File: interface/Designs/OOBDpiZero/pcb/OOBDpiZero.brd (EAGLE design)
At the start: 73.5 x 42 mm, 132 parts, among them IC1 EEPROM24, IC100 LM1117MPX-3.3, IC2 DS3231, Q1 12MHz, U1 MAX98357, U100 SY6280, U101 SN65HVD230(SO8), U102 SN65HVD230(SO8), U2 MP1482

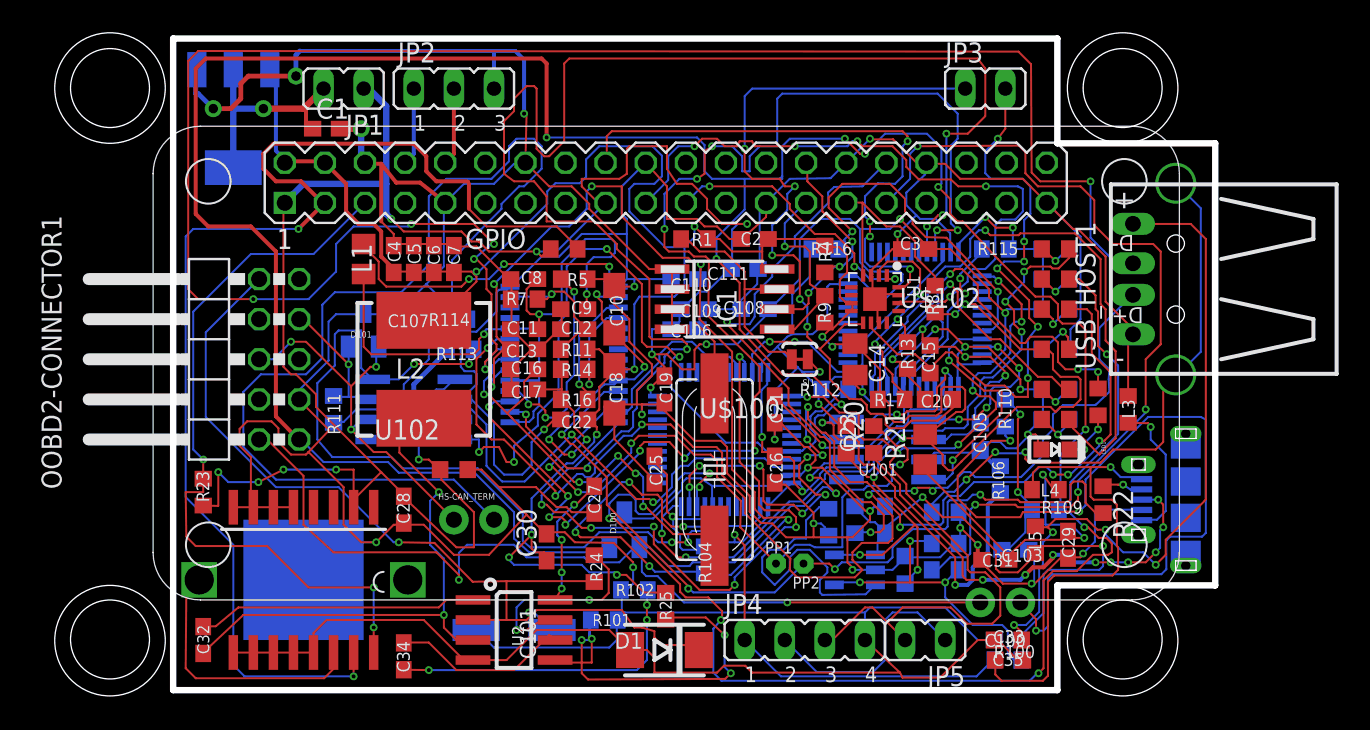
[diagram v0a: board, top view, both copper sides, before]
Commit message: - add design rules check files of different PCB manufacturer - DRC is OK (0 errors) for OOBDpiZero.dru and OSHPark-4layer.dru) - modifications on pizero dimension Library added
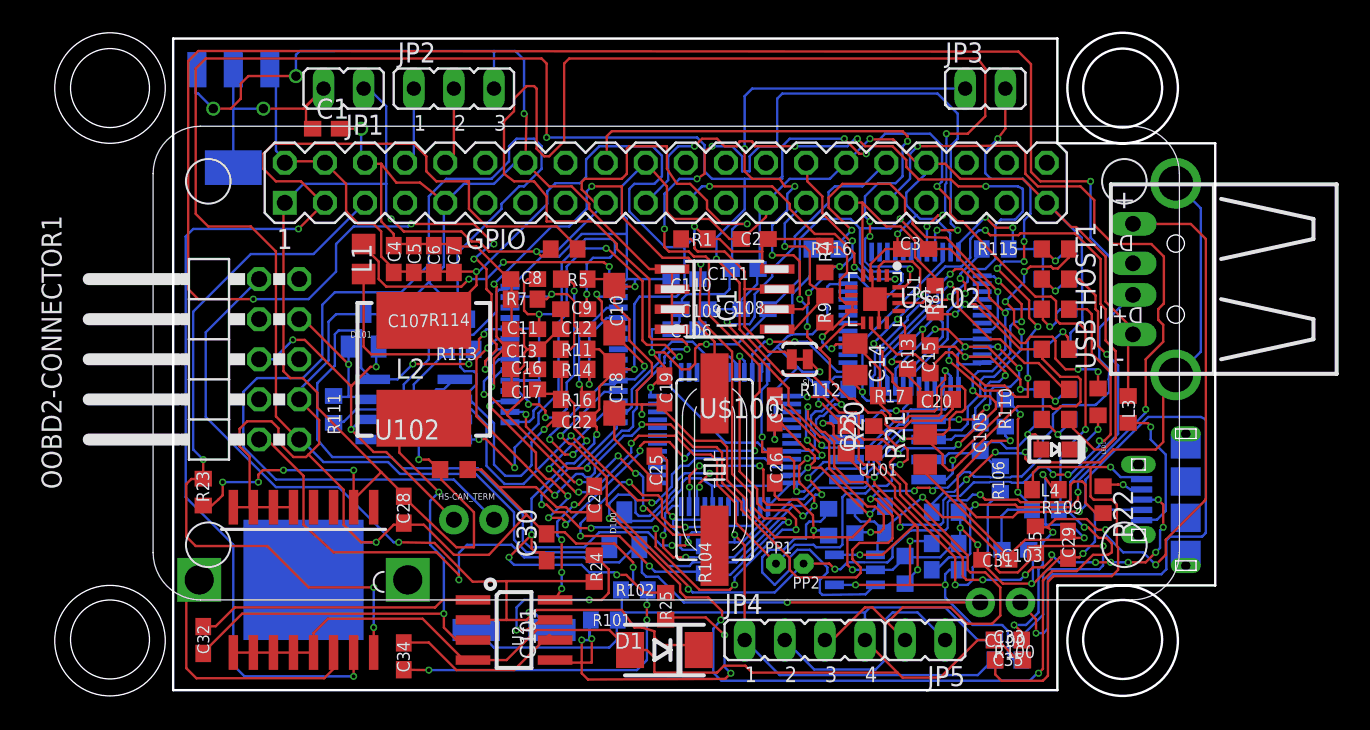
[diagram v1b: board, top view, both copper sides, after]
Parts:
- moved R17 0.24 mm to (45.5, 18.0)
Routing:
- net MS-CAN_L: track 76.4 -> 74.7 mm
- net N$14: track 59.8 -> 58.8 mm
- net USB2_DP: track 76.3 -> 75.6 mm
- net N$18: track 2.71 -> 3.38 mm
- net N$10: track 11.8 -> 12.4 mm
- net N$33: track 45.4 -> 46.0 mm
- net N$39: track 47.5 -> 48.0 mm

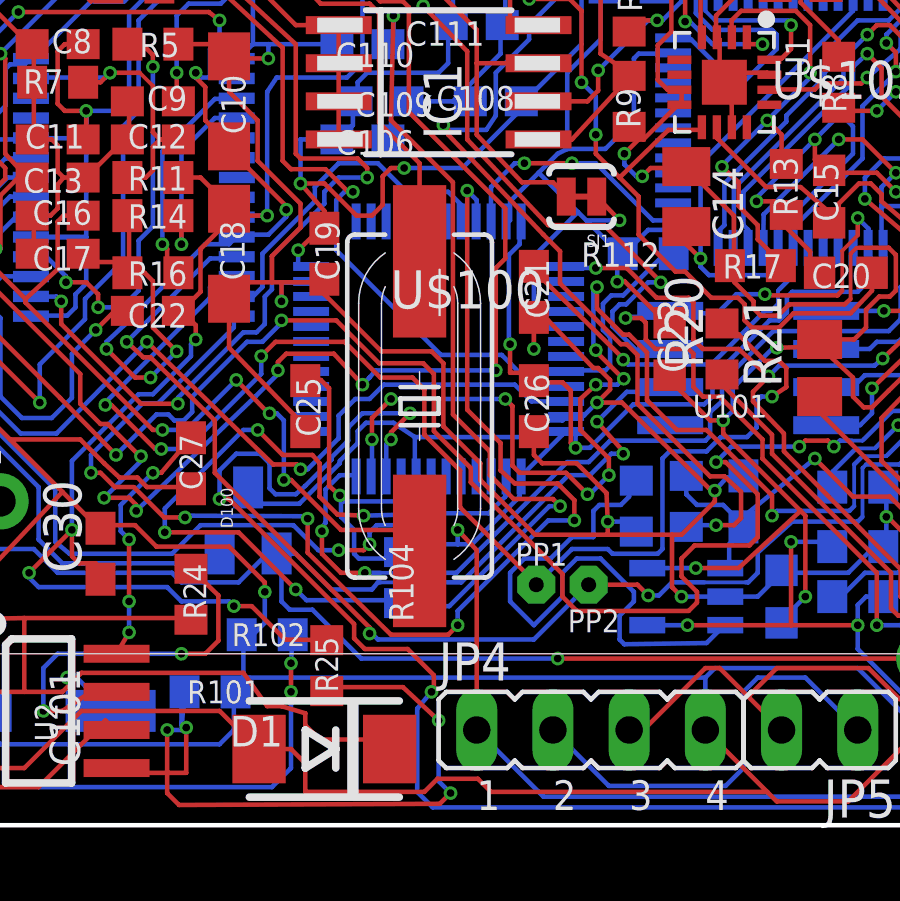
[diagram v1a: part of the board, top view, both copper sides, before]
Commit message: add missing SWDIO routing ---next steps--- 1) optimization for PCB Pool "PCB-POOL HighSpec.dru" 2) modify Power Supply wires to mostly 12mil if possible
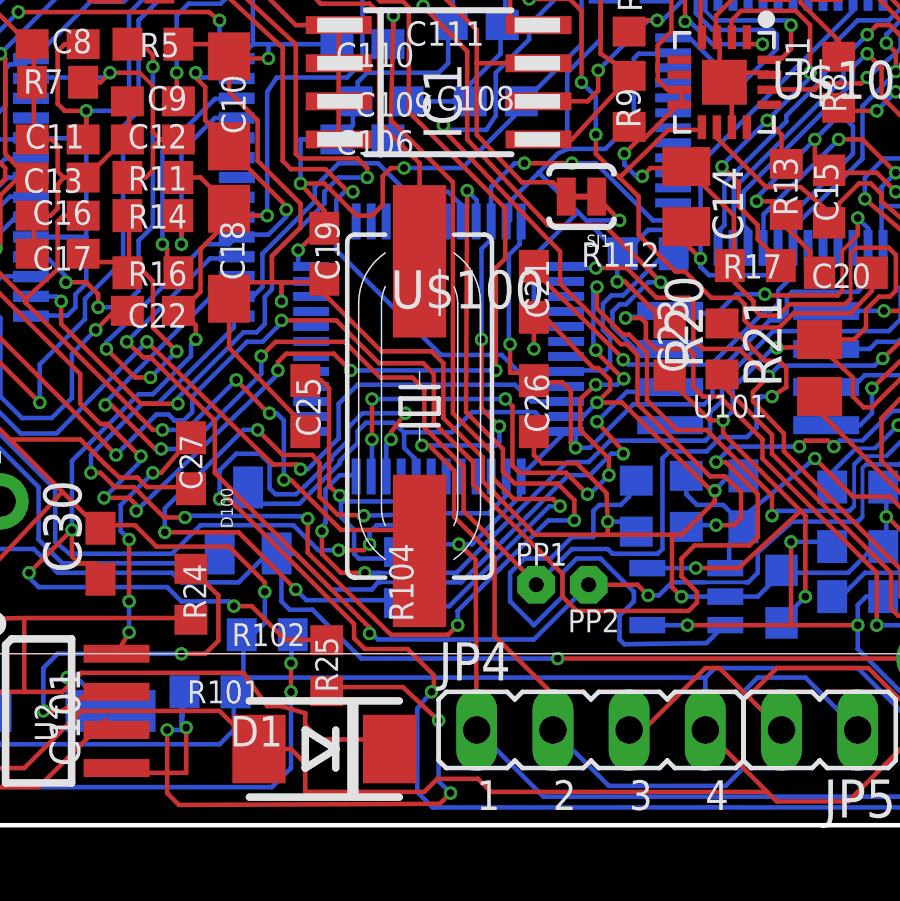
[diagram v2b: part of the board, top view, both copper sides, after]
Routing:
- net SWDIO: track 33.4 -> 55.2 mm, vias 2 -> 5
- net +3V3: track 293.6 -> 292.7 mm

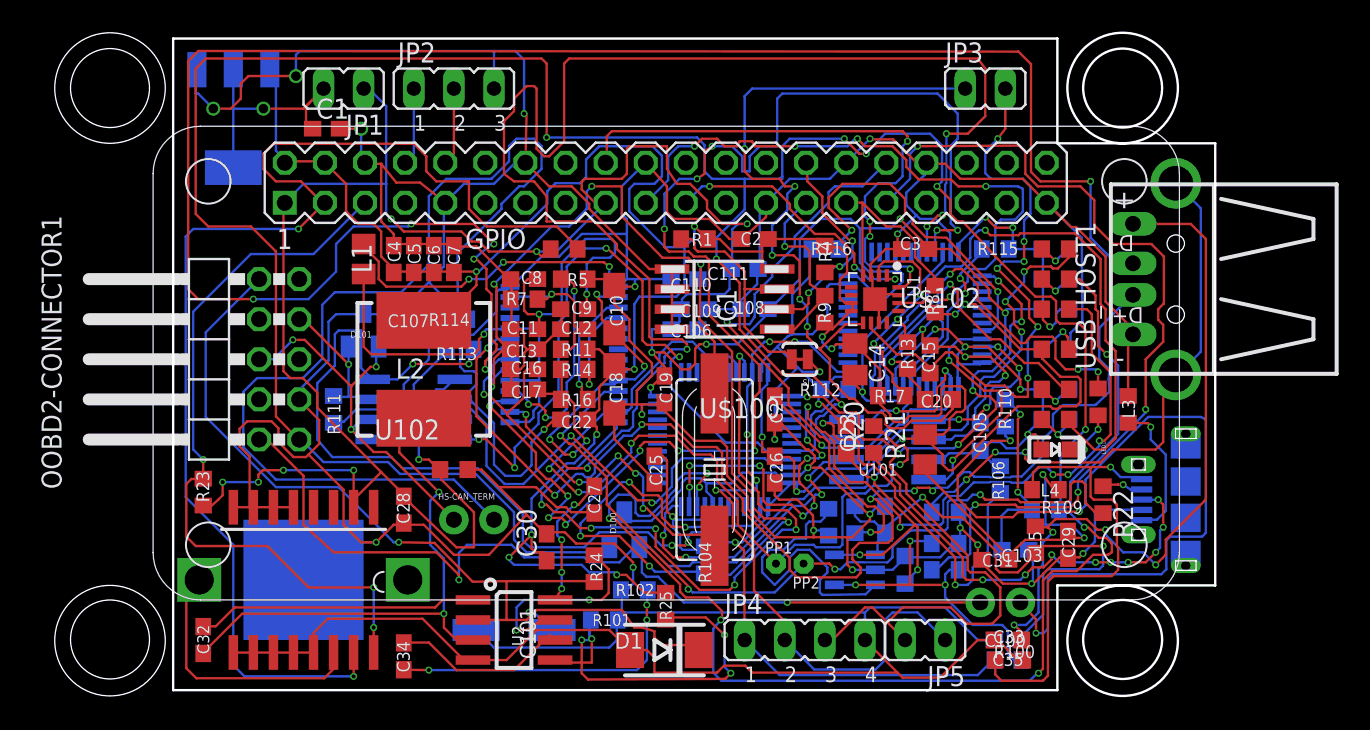
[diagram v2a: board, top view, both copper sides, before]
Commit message: 48 clearance error for "PCB-POOL HighSpec.dru" open !!!optimization ongoing!!! !!!12mil for power supply still open!!!
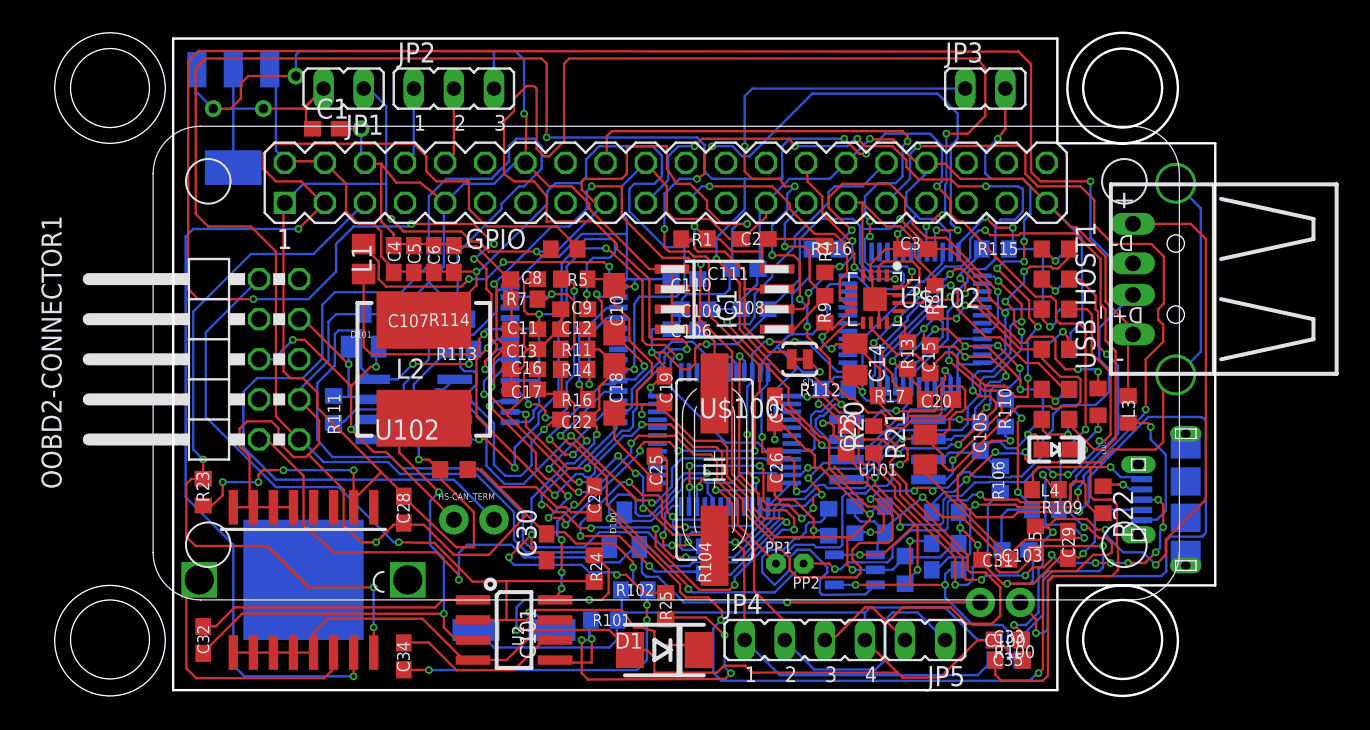
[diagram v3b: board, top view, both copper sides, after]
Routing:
- net N$14: track 59.2 -> 47.1 mm, vias 13 -> 9
- net USB1_DP: track 84.4 -> 80.8 mm
- net GND: track 599.1 -> 600.1 mm
- net N$25: track 2.71 -> 3.48 mm

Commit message: DRC validated against PCB-POOL HighSpec.dru, OSHPark-4layer.dru and OOBDpiZero.dru successfully
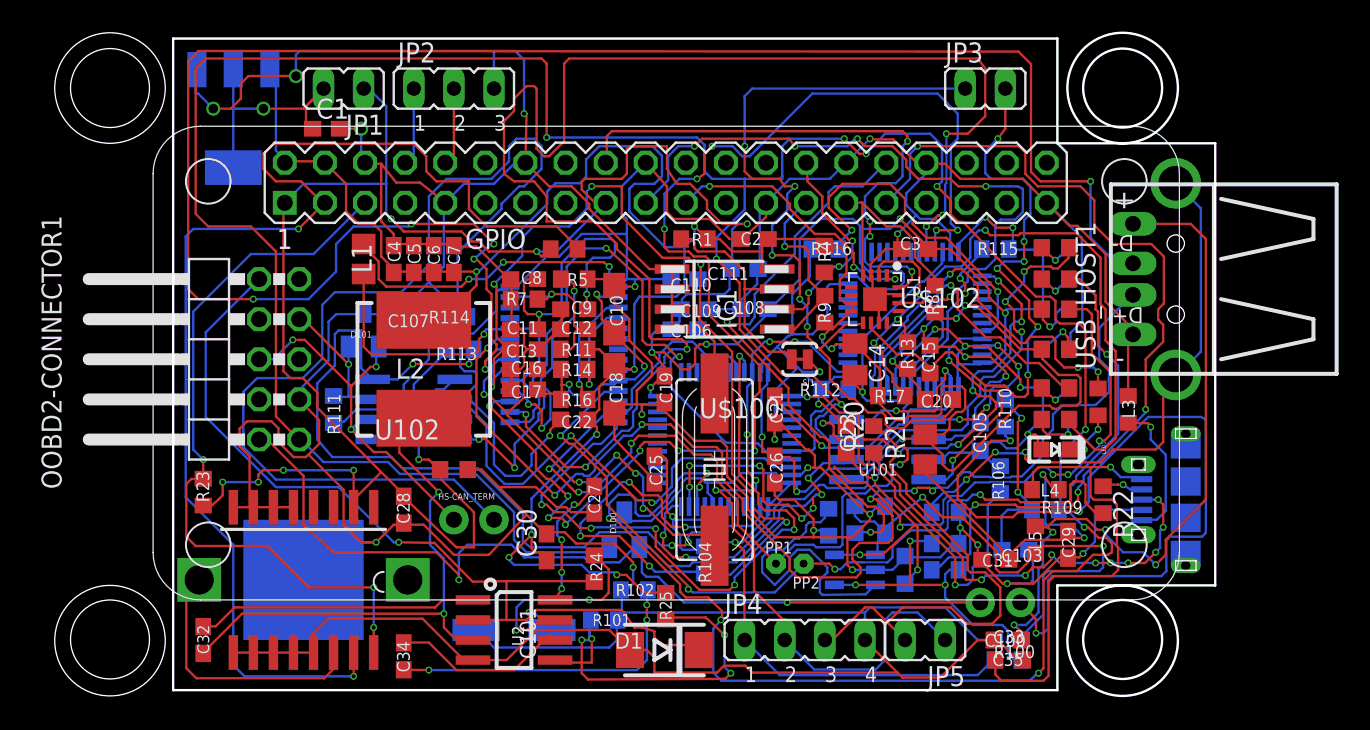
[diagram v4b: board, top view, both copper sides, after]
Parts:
- moved R114 0.16 mm to (17.8, 23.0)
- moved LED101 0.12 mm to (55.9, 18.5)
- moved R15 0.08 mm to (55.9, 18.5)
- moved LED104 0.08 mm to (55.9, 27.4)
- moved R3 0.08 mm to (55.9, 27.4)
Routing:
- net N$33: track 46.0 -> 37.8 mm, vias 8 -> 6
- net N$39: track 48.0 -> 46.7 mm
- net N$40: track 14.0 -> 15.3 mm
- net N$31: track 37.3 -> 37.9 mm
- net HS-CAN_RXD: track 43.2 -> 43.7 mm

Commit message: 1) correct last unrouted wire again 2) start changing GND wires to 12mil
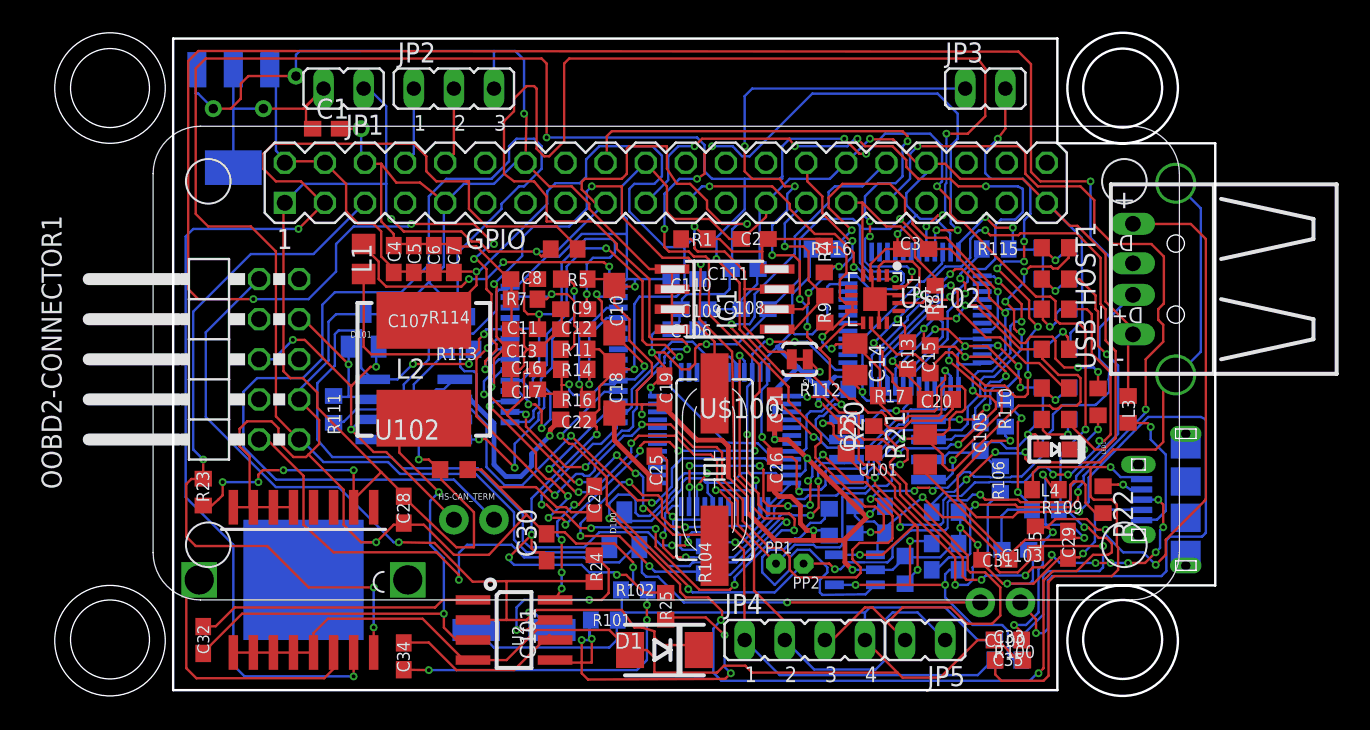
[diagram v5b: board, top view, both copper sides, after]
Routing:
- net N$14: track 47.1 -> 50.3 mm, vias 9 -> 11

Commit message: add modified PCB with 2/3 GND wires set to 12mil
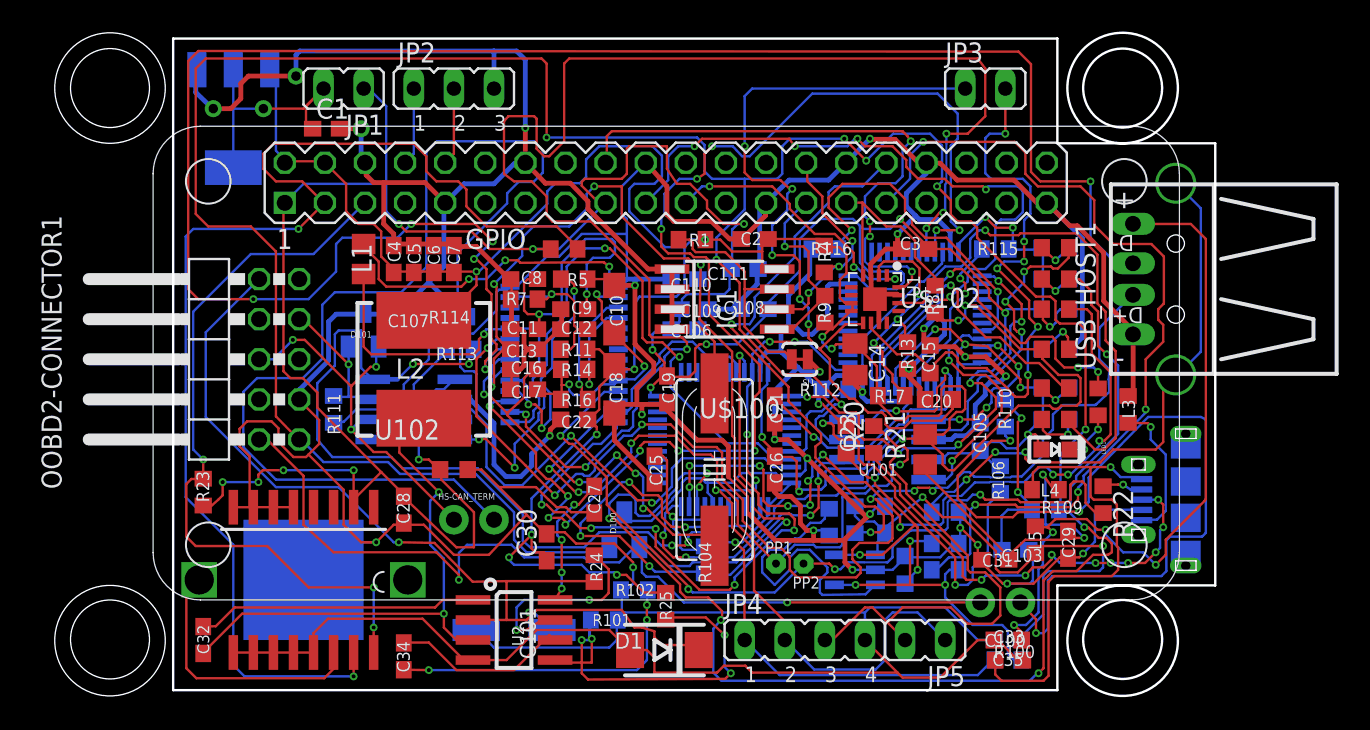
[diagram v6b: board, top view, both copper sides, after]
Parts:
- moved R1 0.16 mm to (32.9, 27.9)
- moved C19 0.16 mm to (31.3, 18.4)
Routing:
- net GND: track 599.5 -> 594.7 mm
- net USB1_DM: track 96.4 -> 92.9 mm
- net N$30: track 65.8 -> 67.2 mm
- net +3V3: track 292.3 -> 290.9 mm
- net +5V: track 190.3 -> 189.4 mm
- net SDA: track 78.2 -> 77.4 mm
- net N$3: track 39.1 -> 39.7 mm
